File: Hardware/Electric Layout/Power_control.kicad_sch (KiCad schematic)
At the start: 18 parts, among them J2 Power IN, J3 CAN BUS Modul, J4 CAN Connect, J5 To USB converter, Q1 IRF9540N, Q2 2N3904

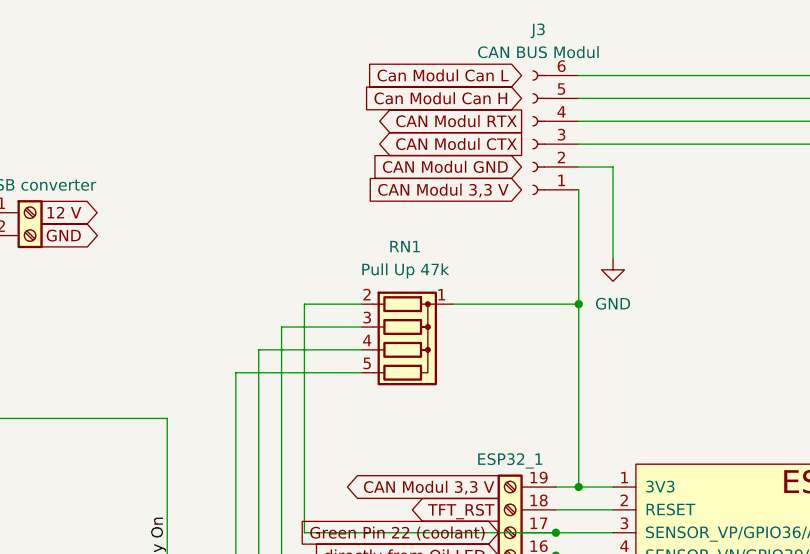
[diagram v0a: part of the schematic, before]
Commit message: Changed Pull up Resistance
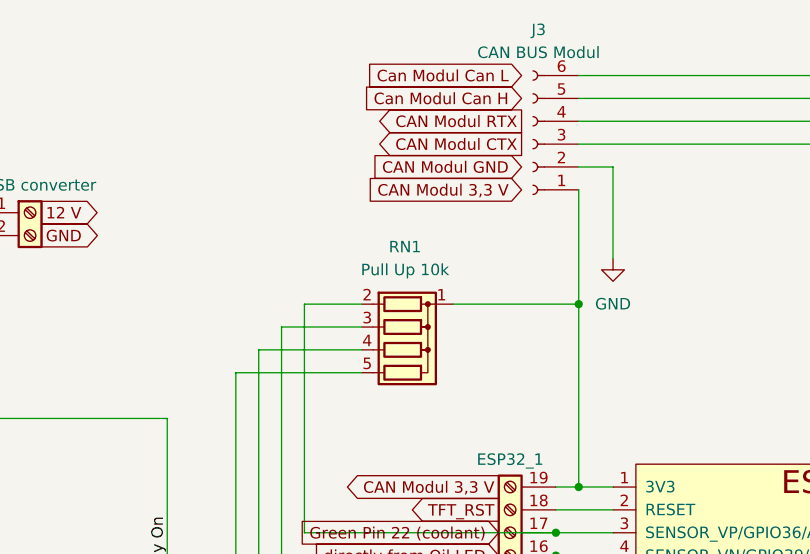
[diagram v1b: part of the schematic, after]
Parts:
- RN1: value Pull Up 47k -> Pull Up 10k
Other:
- company: (none) -> Norbert Schechner
- title: (none) -> T4_MFA Brakeout Board
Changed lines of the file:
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@@
 	(generator_version "8.0")
 	(paper "A4")
+	(title_block
+		(title "T4_MFA Brakeout Board")
+		(date "30.01.2025")
+		(rev "4")
+		(company "Norbert Schechner")
+		(comment 1 "(c) N. Schechner")
+	)
 	(junction
 		(at 160.02 102.87)
@@
 			)
 		)
-		(property "Value" "Pull Up 47k"
+		(property "Value" "Pull Up 10k"
 			(at 143.256 66.04 90)
 			(effects

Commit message: Add files via upload
New layout
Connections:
- net Green Pin 22 (coolant): no longer ESP1.3 (SENSOR_VP/GPIO36/ADC1_CH0), ESP32_1.17 (Pin_17), RN1.2 (R1)
- net Volt Measurement: now also ESP1.4 (SENSOR_VN/GPIO39/ADC1_CH3), ESP32_1.16 (Pin_16); no longer ESP1.7 (32K_XP/GPIO32/ADC1_CH4), ESP32_1.13 (Pin_13)
- net directly from Oil LED: no longer ESP1.4 (SENSOR_VN/GPIO39/ADC1_CH3), ESP32_1.16 (Pin_16), RN1.3 (R2)
- new net: ESP1.3 (SENSOR_VP/GPIO36/ADC1_CH0), ESP32_1.17 (Pin_17), RN1.3 (R2)
- new net: ESP1.7 (32K_XP/GPIO32/ADC1_CH4), ESP32_1.13 (Pin_13)
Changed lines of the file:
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@@
 	)
 	(junction
-		(at 160.02 105.41)
+		(at 50.8 59.69)
+		(diameter 0)
+		(color 0 0 0 0)
+	)
+	(junction
+		(at 57.15 96.52)
+		(diameter 0)
+		(color 0 0 0 0)
+	)
+	(junction
+		(at 69.85 82.55)
 		(diameter 0)
 		(color 0 0 0 0)
@@
 	)
 	(junction
-		(at 50.8 59.69)
-		(diameter 0)
-		(color 0 0 0 0)
-	)
-	(junction
-		(at 57.15 96.52)
-		(diameter 0)
-		(color 0 0 0 0)
-	)
-	(junction
-		(at 69.85 82.55)
-		(diameter 0)
-		(color 0 0 0 0)
-	)
-	(junction
 		(at 162.56 90.17)
 		(diameter 0)
@@
 	(wire
 		(pts
-			(xy 57.15 105.41) (xy 160.02 105.41)
-		)
-		(stroke
-			(width 0)
-			(type default)
-		)
-	)
-	(wire
-		(pts
 			(xy 81.28 82.55) (xy 83.82 82.55)
 		)
@@
 	(wire
 		(pts
+			(xy 129.54 95.25) (xy 160.02 95.25)
+		)
+		(stroke
+			(width 0)
+			(type default)
+		)
+	)
+	(wire
+		(pts
 			(xy 237.49 115.57) (xy 231.14 115.57)
 		)
@@
 	(wire
 		(pts
+			(xy 105.41 105.41) (xy 105.41 97.79)
+		)
+		(stroke
+			(width 0)
+			(type default)
+		)
+	)
+	(wire
+		(pts
 			(xy 162.56 44.45) (xy 232.41 44.45)
 		)
@@
 	(wire
 		(pts
+			(xy 138.43 72.39) (xy 129.54 72.39)
+		)
+		(stroke
+			(width 0)
+			(type default)
+		)
+	)
+	(wire
+		(pts
 			(xy 25.4 59.69) (xy 50.8 59.69)
 		)
@@
 	(wire
 		(pts
-			(xy 132.08 69.85) (xy 138.43 69.85)
+			(xy 129.54 72.39) (xy 129.54 95.25)
 		)
 		(stroke
@@
 	(wire
 		(pts
-			(xy 132.08 95.25) (xy 160.02 95.25)
-		)
-		(stroke
-			(width 0)
-			(type default)
-		)
-	)
-	(wire
-		(pts
 			(xy 41.91 96.52) (xy 45.72 96.52)
 		)
@@
 	(wire
 		(pts
+			(xy 160.02 95.25) (xy 166.37 95.25)
+		)
+		(stroke
+			(width 0)
+			(type default)
+		)
+	)
+	(wire
+		(pts
 			(xy 237.49 125.73) (xy 231.14 125.73)
 		)
@@
 	(wire
 		(pts
+			(xy 105.41 97.79) (xy 160.02 97.79)
+		)
+		(stroke
+			(width 0)
+			(type default)
+		)
+	)
+	(wire
+		(pts
 			(xy 148.59 69.85) (xy 162.56 69.85)
 		)
@@
 	(wire
 		(pts
-			(xy 129.54 72.39) (xy 138.43 72.39)
-		)
-		(stroke
-			(width 0)
-			(type default)
-		)
-	)
-	(wire
-		(pts
 			(xy 166.37 90.17) (xy 162.56 90.17)
 		)
@@
 	(wire
 		(pts
+			(xy 160.02 97.79) (xy 166.37 97.79)
+		)
+		(stroke
+			(width 0)
+			(type default)
+		)
+	)
+	(wire
+		(pts
 			(xy 62.23 82.55) (xy 69.85 82.55)
 		)
@@
 	(wire
 		(pts
-			(xy 129.54 72.39) (xy 129.54 97.79)
-		)
-		(stroke
-			(width 0)
-			(type default)
-		)
-	)
-	(wire
-		(pts
 			(xy 116.84 82.55) (xy 116.84 120.65)
 		)
@@
 	(wire
 		(pts
-			(xy 129.54 97.79) (xy 160.02 97.79)
-		)
-		(stroke
-			(width 0)
-			(type default)
-		)
-	)
-	(wire
-		(pts
 			(xy 237.49 100.33) (xy 231.14 100.33)
 		)
@@
 	(wire
 		(pts
-			(xy 160.02 97.79) (xy 166.37 97.79)
-		)
-		(stroke
-			(width 0)
-			(type default)
-		)
-	)
-	(wire
-		(pts
 			(xy 160.02 105.41) (xy 166.37 105.41)
 		)
@@
 	(wire
 		(pts
-			(xy 132.08 95.25) (xy 132.08 69.85)
-		)
-		(stroke
-			(width 0)
-			(type default)
-		)
-	)
-	(wire
-		(pts
 			(xy 236.22 102.87) (xy 237.49 102.87)
 		)
@@
 	(wire
 		(pts
-			(xy 160.02 95.25) (xy 166.37 95.25)
-		)
-		(stroke
-			(width 0)
-			(type default)
-		)
-	)
-	(wire
-		(pts
 			(xy 41.91 96.52) (xy 41.91 134.62)
 		)
@@
 		(pts
 			(xy 127 74.93) (xy 127 100.33)
+		)
+		(stroke
+			(width 0)
+			(type default)
+		)
+	)
+	(wire
+		(pts
+			(xy 57.15 105.41) (xy 105.41 105.41)
 		)
 		(stroke
@@
 	(global_label "directly from Oil LED"
 		(shape input)
-		(at 153.67 97.79 180)
-		(fields_autoplaced yes)
-		(effects
-			(font
-				(size 1.27 1.27)
-			)
-			(justify right)
-		)
-		(property "Intersheetrefs" "${INTERSHEET_REFS}"
-			(at 130.3045 97.79 0)
+		(at 153.67 110.49 180)
+		(fields_autoplaced yes)
+		(effects
+			(font
+				(size 1.27 1.27)
+			)
+			(justify right)
+		)
+		(property "Intersheetrefs" "${INTERSHEET_REFS}"
+			(at 130.3045 110.49 0)
 			(effects
 				(font
@@
 	(global_label "Green Pin 22 (coolant)"
 		(shape input)
-		(at 153.67 95.25 180)
-		(fields_autoplaced yes)
-		(effects
-			(font
-				(size 1.27 1.27)
-			)
-			(justify right)
-		)
-		(property "Intersheetrefs" "${INTERSHEET_REFS}"
-			(at 128.1879 95.25 0)
-			(effects
-				(font
-					(size 1.27 1.27)
-				)
-				(justify right)
+		(at 243.84 123.19 0)
+		(fields_autoplaced yes)
+		(effects
+			(font
+				(size 1.27 1.27)
+			)
+			(justify left)
+		)
+		(property "Intersheetrefs" "${INTERSHEET_REFS}"
+			(at 269.3221 123.19 0)
+			(effects
+				(font
+					(size 1.27 1.27)
+				)
+				(justify left)
 				(hide yes)
 			)
@@
 		(property "Intersheetrefs" "${INTERSHEET_REFS}"
 			(at 136.5943 44.45 0)
-			(effects
-				(font
-					(size 1.27 1.27)
-				)
-				(justify right)
-				(hide yes)
-			)
-		)
-	)
-	(global_label "Pin 21 (Door Left)"
-		(shape input)
-		(at 153.67 110.49 180)
-		(fields_autoplaced yes)
-		(effects
-			(font
-				(size 1.27 1.27)
-			)
-			(justify right)
-		)
-		(property "Intersheetrefs" "${INTERSHEET_REFS}"
-			(at 132.7235 110.49 0)
 			(effects
 				(font
@@
 	(global_label "Green Pin 6 (Wiper Water))"
 		(shape input)
-		(at 243.84 128.27 0)
-		(fields_autoplaced yes)
-		(effects
-			(font
-				(size 1.27 1.27)
-			)
-			(justify left)
-		)
-		(property "Intersheetrefs" "${INTERSHEET_REFS}"
-			(at 273.1323 128.27 0)
-			(effects
-				(font
-					(size 1.27 1.27)
-				)
-				(justify left)
-				(hide yes)
-			)
+		(at 153.67 105.41 180)
+		(fields_autoplaced yes)
+		(effects
+			(font
+				(size 1.27 1.27)
+			)
+			(justify right)
+		)
+		(property "Intersheetrefs" "${INTERSHEET_REFS}"
+			(at 124.3777 105.41 0)
+			(effects
+				(font
+					(size 1.27 1.27)
+				)
+				(justify right)
+				(hide yes)
+			)
